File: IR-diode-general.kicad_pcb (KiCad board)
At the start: 2 copper layers, 80 x 20.5 mm, 39 parts, among them J1 BarrelJack_3167288, J2 USB4105-GF-A, U1 QFN10_MP2483DQ_MNP, U2 AP62301Z6-7, U3 SM02B-SRSS-TB-LF-SN, U4 SM02B-SRSS-TB-LF-SN

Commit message: Added signage
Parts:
- added N1: antmicro_logo, antmicro-footprints:antmicro-logo_scaled_12mm, B.Cu at (127.2, 44.8)
- U1: value QFN10_MP2483DQ_MNP -> MP2483DQ-LF-P
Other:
- board text added: "1050nm IR LED Driver rev.1.0.0 04/2023"

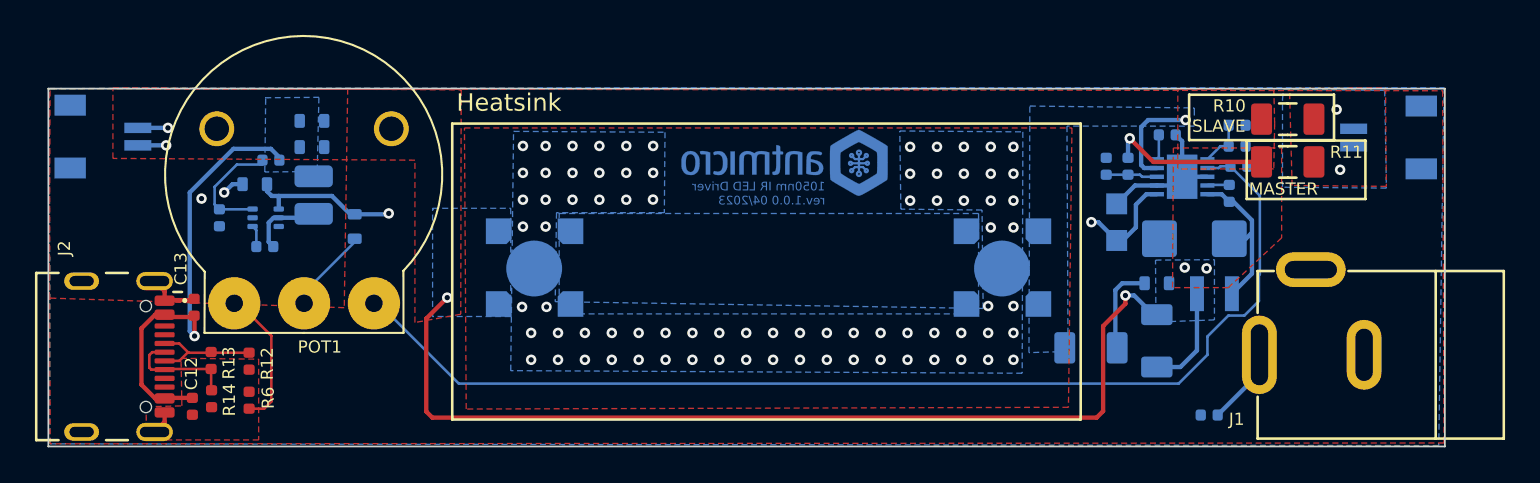
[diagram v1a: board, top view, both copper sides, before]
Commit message: Added OSHW marking
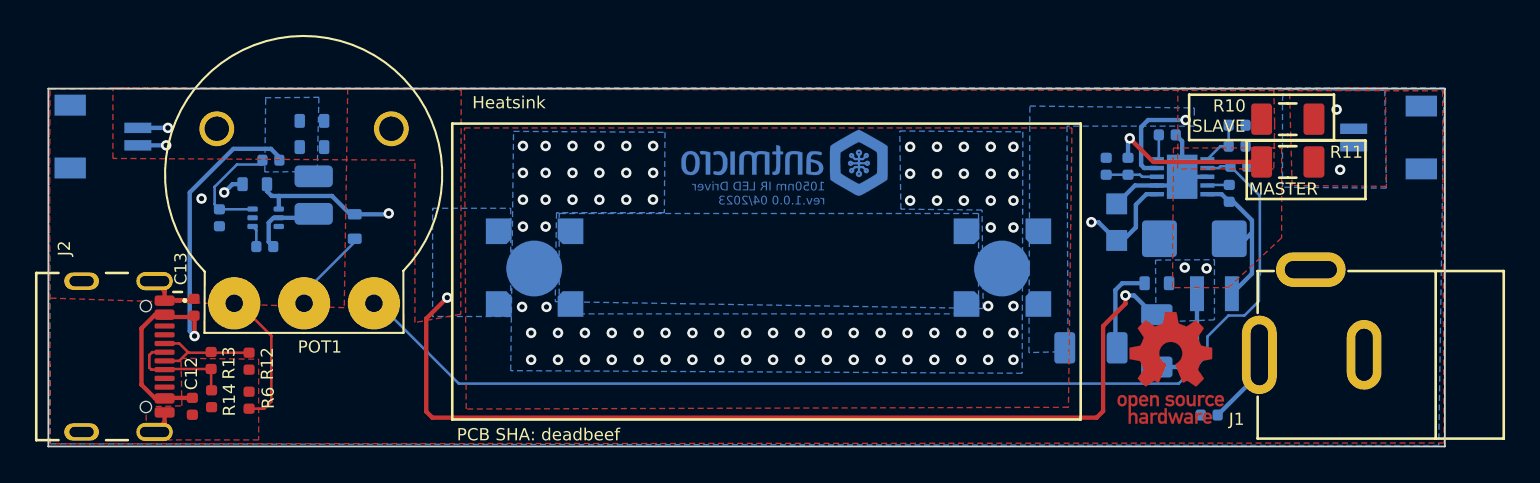
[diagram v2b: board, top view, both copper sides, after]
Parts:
- added N2: oshw_logo, antmicro-footprints:oshw-logo, F.Cu at (149.3, 56.5)
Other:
- board text added: "PCB SHA: deadbeef"
